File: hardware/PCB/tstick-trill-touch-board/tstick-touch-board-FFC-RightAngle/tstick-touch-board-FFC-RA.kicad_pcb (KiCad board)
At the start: 2 copper layers, 102.5 x 28 mm, 12 parts, among them J1 Conn_01x32

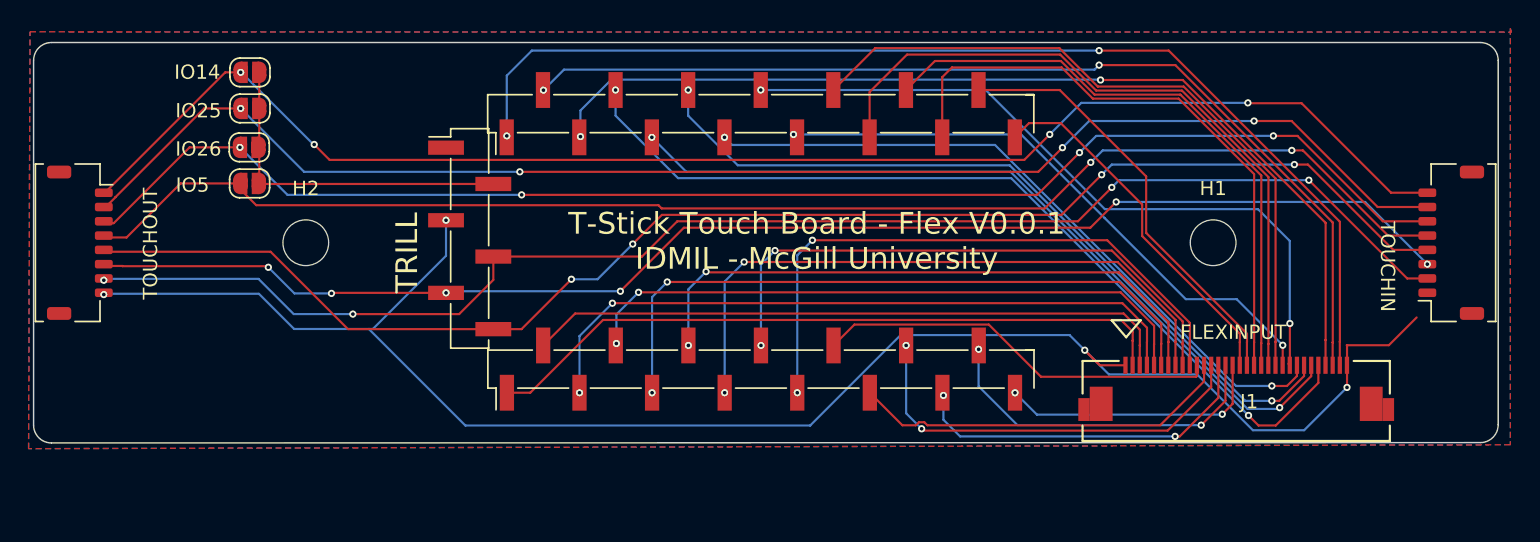
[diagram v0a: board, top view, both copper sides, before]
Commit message: cleaned up the pcb designs for the touch extension boards, created BOM and gerber files for fabrication and assembly
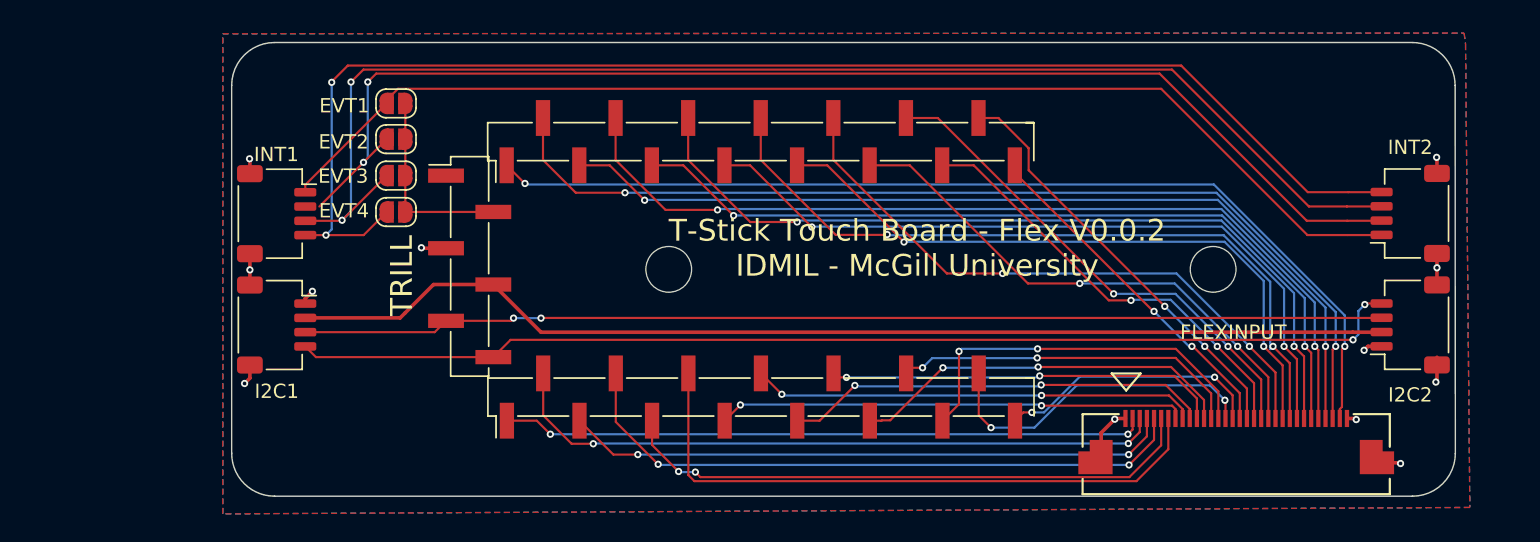
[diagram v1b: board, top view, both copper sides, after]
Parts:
- removed TrillExtensionInput1, TrillExtensionOutput2: Conn_01x08, Connector_JST:JST_SHL_SM08B-SHLS-TF_1x08-1MP_P1.00mm_Horizontal
- added I2C1: Conn_01x04, Connector_JST:JST_SH_SM04B-SRSS-TB_1x04-1MP_P1.00mm_Horizontal, F.Cu at (135.8, 98.0)
- added I2C2: Conn_01x04, Connector_JST:JST_SH_SM04B-SRSS-TB_1x04-1MP_P1.00mm_Horizontal, F.Cu at (215.1, 98.0)
- added INT1: Conn_01x04, Connector_JST:JST_SH_SM04B-SRSS-TB_1x04-1MP_P1.00mm_Horizontal, F.Cu at (135.8, 90.2)
- added INT2: Conn_01x04, Connector_JST:JST_SH_SM04B-SRSS-TB_1x04-1MP_P1.00mm_Horizontal, F.Cu at (215.1, 90.2)
- J1: footprint molex_ffc_footprints:CON_541323262_MOL -> molex-ffc-connectors:CON_541323262_MOL
- moved H2 25.5 mm to (163.2, 94.1)
- moved JP4 14.1 mm to (144.1, 90.1)
- moved JP1 11.7 mm to (144.1, 82.5)
- moved JP3 11.2 mm to (144.1, 87.6)
- moved JP2 10.3 mm to (144.1, 85.0)
- moved J1 3.72 mm to (202.9, 107.1)
- moved TOUCH3 1.96 mm to (149.3, 93.9)
- moved TOUCH1 1.96 mm to (169.7, 103.1)
- moved TOUCH2 1.96 mm to (169.6, 85.2)
- moved H1 1.86 mm to (201.3, 94.1)
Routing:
- net GND: track 119.4 -> 22.0 mm, vias 4 -> 12
- net /SCL: track 102.1 -> 78.2 mm, vias 4 -> 2
- net +3V3: track 101.4 -> 77.7 mm, vias 4 -> 0
- net /SDA: track 97.9 -> 75.7 mm, vias 6 -> 2
- net /EVT1: track 99.3 -> 83.1 mm, vias 2 -> 0
- net /TOUCH8: track 42.9 -> 29.9 mm
- net /EVT2: track 100.4 -> 87.9 mm, vias 4 -> 2
- net /TOUCH17: track 42.8 -> 30.6 mm, vias 0 -> 2
- net /TOUCH19: track 48.9 -> 36.9 mm, vias 0 -> 2
- net /TOUCH6: track 44.8 -> 32.8 mm
- net /TRILL_EVT: track 24.2 -> 13.8 mm
- net /TOUCH7: track 40.7 -> 31.2 mm
- net /EVT4: track 102.9 -> 94.9 mm, vias 4 -> 2
- net /TOUCH29: track 78.4 -> 70.4 mm
- net /EVT3: track 101.3 -> 93.4 mm, vias 4 -> 2
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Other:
- board size 102.5 x 28 mm -> 85.6 x 31.8 mm
- board text added: "EVT1"
- board text added: "EVT2"
- board text added: "EVT3"
- board text added: "EVT4"
- board text added: "T-Stick Touch Board - Flex V0.0.2 IDMIL - McGill University"
- board text removed: "IO14"
- board text removed: "IO25"
- board text removed: "IO26"
- board text removed: "IO5"
- board text removed: "T-Stick Touch Board - Flex V0.0.1 IDMIL - McGill University"
- board text removed: "TOUCHIN"
- board text removed: "TOUCHOUT"

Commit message: updated BOM for 5gw board, updated silkscreen for touch board
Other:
- board text added: "T-Stick Touch Board - Flex V1.0.0 IDMIL - McGill University"
- board text removed: "T-Stick Touch Board - Flex V0.0.2 IDMIL - McGill University"
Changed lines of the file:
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@@
     (effects (font (size 1 1) (thickness 0.15)) (justify left bottom))
   )
-  (gr_text "FLEXINPUT" (at 202.7174 98.5266) (layer "F.SilkS")
+  (gr_text "FLEXINPUT" (at 206.7392 101.973) (layer "F.SilkS")
     (effects (font (size 1 1) (thickness 0.15)))
   )
-  (gr_text "T-Stick Touch Board - Flex V0.0.2\nIDMIL - McGill University" (at 180.5892 92.638) (layer "F.SilkS")
+  (gr_text "T-Stick Touch Board - Flex V1.0.0\nIDMIL - McGill University" (at 180.5892 92.638) (layer "F.SilkS")
     (effects (font (size 1.524 1.524) (thickness 0.2032)))
   )
